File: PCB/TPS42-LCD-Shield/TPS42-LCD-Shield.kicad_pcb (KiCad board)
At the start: 2 copper layers, 17.7 x 25.8 mm, 16 parts, among them J7 FH12-10S-0.5SH, J8 Conn_01x06

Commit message: finalizing
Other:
- board text added: "${Revision}"
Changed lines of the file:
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@@
     )
   )
+  (property "Revision" "1.0")
   (net 0 "")
   (net 1 "/L_DAT")
@@
     (effects (font (size 0.75 0.75) (thickness 0.1)) (justify mirror))
   )
+  (gr_text "${Revision}" (at 95.75 37.25) (layer "F.SilkS")
+    (effects (font (size 1 1) (thickness 0.15)))
+  )
   (gr_text "Right" (at 95.52 50.8 90) (layer "F.SilkS")

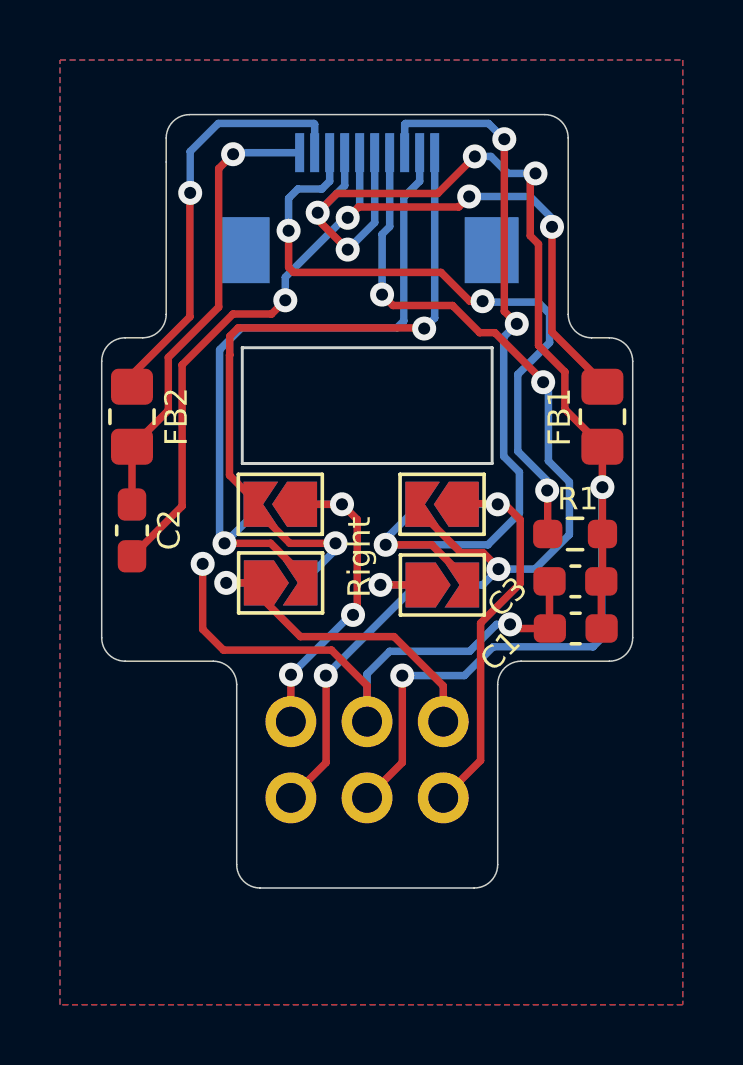
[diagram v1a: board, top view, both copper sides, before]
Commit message: reduced with and added longer pads for fcc
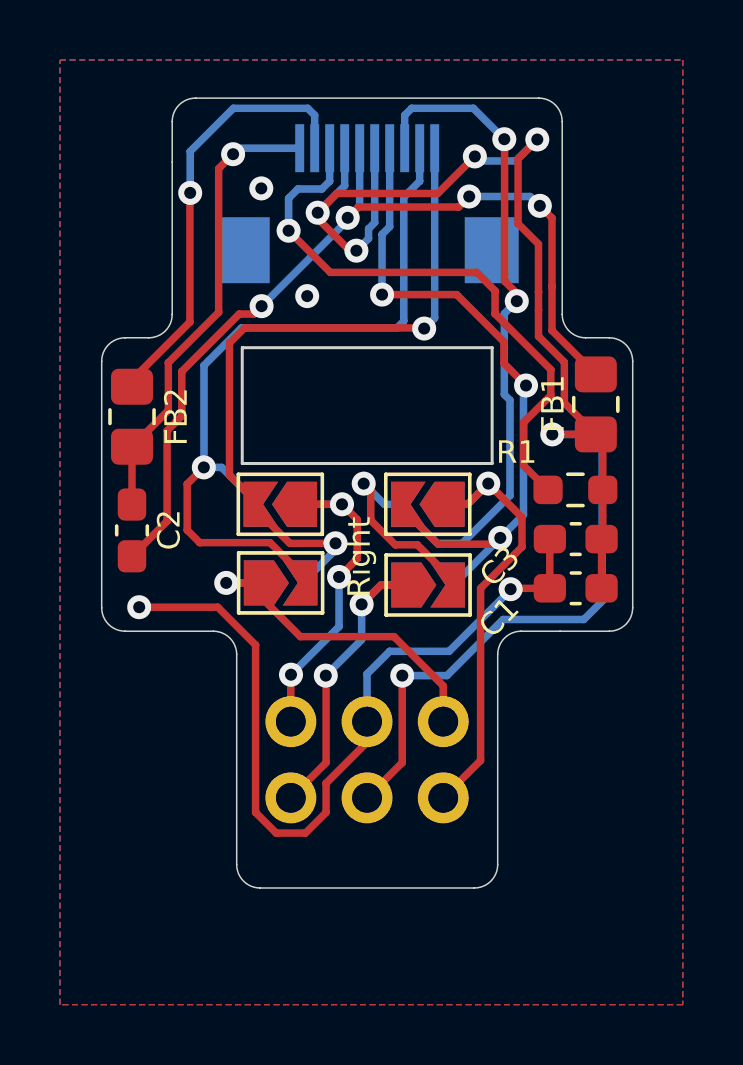
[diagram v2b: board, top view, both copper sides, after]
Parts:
- moved R1 1.47 mm to (102.7, 48.6)
- moved C3 1.41 mm to (102.7, 50.2)
- moved C1 1.34 mm to (102.7, 51.8)
- moved JP1 0.48 mm to (97.8, 51.7)
- moved JP2 0.48 mm to (97.8, 49.0)
- moved JP5 0.48 mm to (97.8, 51.7)
- moved JP6 0.48 mm to (97.8, 49.0)
- moved FB1 0.47 mm to (103.4, 45.7)
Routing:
- net GND: track 33.8 -> 41.7 mm, vias 3 -> 5
- net +3V3: track 48.9 -> 53.5 mm
- net /L_EXTMODE: track 22.4 -> 19.6 mm, vias 3 -> 1
- net /L_DAT: track 24.0 -> 26.0 mm
- net /L_EIN: track 24.8 -> 23.2 mm
- net /L_CS: track 27.6 -> 28.8 mm
- net Net-(J8-Pad4): track 13.6 -> 14.7 mm
- net VDDA: track 31.1 -> 30.2 mm
- net Net-(J8-Pad6): track 11.7 -> 10.9 mm
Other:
- board size 17.7 x 25.8 mm -> 17.7 x 26.3 mm
